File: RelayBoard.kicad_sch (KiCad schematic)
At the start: 103 parts, among them J1 CONN_03-SCREW-5MM, J11 CONN_03-SCREW-5MM, J12 CONN_03-SCREW-5MM, J13 CONN_03-SCREW-5MM, J14 CONN_03-SCREW-5MM, J15 CONN_03-SCREW-5MM, J16 CONN_03-SCREW-5MM, J17 CONN_03-SCREW-5MM, J18 CONN_03-SCREW-5MM, J2 CONN_03-SCREW-5MM, J22 Conn_01x04, J3 CONN_03-SCREW-5MM, J4 CONN_03-SCREW-5MM, J5 CONN_03-SCREW-5MM, J6 CONN_03-SCREW-5MM, J7 CONN_03-SCREW-5MM, J8 CONN_03-SCREW-5MM, J9 PJ-202A, Q1 ULN2803ADWR, Q2 ULN2803ADWR, U1 TLP148G, U11 TLP148G, U12 TLP148G, U13 TLP148G, U14 TLP148G, U15 TLP148G, U16 TLP148G, U17 TLP148G, U18 TLP148G, U2 TLP148G, U3 TLP148G, U4 TLP148G, U5 TLP148G, U6 TLP148G, U7 TLP148G, U8 TLP148G

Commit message: final touches
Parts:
- gave numbers to parts that had none: 1
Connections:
- net DC In from AC: now reaches JP1.3 (Pin_3), PS1.4 (+Vo)
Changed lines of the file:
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@@
   (junction (at 260.096 18.542) (diameter 0) (color 0 0 0 0)
   )
+  (junction (at 51.308 162.306) (diameter 0) (color 0 0 0 0)
+  )
   (junction (at 100.0115 226.06) (diameter 0) (color 0 0 0 0)
   )
@@
     (stroke (width 0) (type default) (color 0 0 0 0))
   )
+  (wire (pts (xy 51.308 165.608) (xy 51.308 162.306))
+    (stroke (width 0) (type default) (color 0 0 0 0))
+  )
   (wire (pts (xy 210.82 155.956) (xy 210.82 155.702))
     (stroke (width 0) (type default) (color 0 0 0 0))
@@
     (stroke (width 0) (type default) (color 0 0 0 0))
   )
+  (wire (pts (xy 51.308 162.306) (xy 51.562 162.306))
+    (stroke (width 0) (type default) (color 0 0 0 0))
+  )
   (polyline (pts (xy 140.97 136.906) (xy 140.97 170.561))
     (stroke (width 0.254) (type solid) (color 0 0 0 0))
@@
     (stroke (width 0) (type default) (color 0 0 0 0))
   )
-  (wire (pts (xy 49.022 162.306) (xy 51.562 162.306))
+  (wire (pts (xy 49.022 162.306) (xy 51.308 162.306))
     (stroke (width 0) (type default) (color 0 0 0 0))
   )
@@
     (stroke (width 0) (type default) (color 0 0 0 0))
   )
+  (wire (pts (xy 53.848 165.608) (xy 51.308 165.608))
+    (stroke (width 0) (type default) (color 0 0 0 0))
+  )
   (polyline (pts (xy 140.97 170.561) (xy 14.732 170.434))
     (stroke (width 0.254) (type solid) (color 0 0 0 0))
@@
     (effects (font (size 3.9878 3.9878)) (justify left bottom))
   )
+  (global_label "DC In from AC" (shape input) (at 53.848 165.608 0) (fields_autoplaced)
+    (effects (font (size 1.27 1.27)) (justify left))
+    (property "Intersheet References" "${INTERSHEET_REFS}" (id 0) (at 70.1706 165.5286 0)
+      (effects (font (size 1.27 1.27)) (justify left) hide)
+    )
+  )
   (global_label "I2C_SDA" (shape bidirectional) (at 140.716 69.85 0) (fields_autoplaced)
     (effects (font (size 1.27 1.27)) (justify left))
@@
   (symbol (lib_id "Connector:Screw_Terminal_01x02") (at 19.558 165.862 180) (unit 1)
     (in_bom yes) (on_board yes)
-    (property "Reference" "J?" (id 0) (at 19.304 158.496 0))
+    (property "Reference" "J10" (id 0) (at 19.304 158.496 0))
     (property "Value" "" (id 1) (at 19.558 160.274 0))
     (property "Footprint" "" (id 2) (at 19.558 165.862 0)
@@
       (effects (font (size 1.27 1.27)) hide)
     )
-    (property "Value" "GND" (id 1) (at 54.102 168.656 0))
+    (property "Value" "GND" (id 1) (at 52.324 169.164 0))
     (property "Footprint" "" (id 2) (at 49.022 167.386 0)
       (effects (font (size 1.27 1.27)) hide)
@@
       (reference "J9") (unit 1) (value "PJ-202A") (footprint "Connectors:POWER_JACK_PTH_LOCK")
     )
+    (path "/2c0c12a9-f7a0-4389-a8c1-bd69df364647"
+      (reference "J10") (unit 1) (value "AC In") (footprint "TerminalBlock:TerminalBlock_Altech_AK300-2_P5.00mm")
+    )
     (path "/04a15d9e-6cd5-4e20-ab11-6766c342d625"
       (reference "J11") (unit 1) (value "CONN_03-SCREW-5MM") (footprint "Connectors:SCREWTERMINAL-5MM-3")
@@
       (reference "J22") (unit 1) (value "Conn_01x04") (footprint "Connector_PinSocket_2.54mm:PinSocket_1x04_P2.54mm_Vertical")
     )
-    (path "/2c0c12a9-f7a0-4389-a8c1-bd69df364647"
-      (reference "J?") (unit 1) (value "AC In") (footprint "TerminalBlock:TerminalBlock_Altech_AK300-2_P5.00mm")
-    )
     (path "/d43d6827-1e42-4d7c-85a8-2e3c7801a7de"

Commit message: total rewrite, solid state relays & change all footprints to 0805s
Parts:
- removed J1, J11, J12, J13, J14, J15, J16, J17, J18, J2, J3, J4, J5, J6, J7, J8: CONN_03-SCREW-5MM, Connectors:SCREWTERMINAL-5MM-3, symbol SparkFun-Connectors:CONN_03-SCREW-5MM
- removed PS1: (no value), symbol Converter_ACDC:IRM-02-5
- removed Q1, Q2: ULN2803ADWR, digikey-footprints:SOIC-18_W7.5mm, symbol dk_Transistors-Bipolar-BJT-Arrays:ULN2803ADWR
- removed U1, U11, U12, U13, U14, U15, U16, U17, U18, U2, U3, U4, U5, U6, U7, U8: TLP148G, Package_SO:MFSOP6-5_4.4x3.6mm_P1.27mm, symbol Relay_SolidState:TLP148G
- removed UP1: AP1117-33, Package_TO_SOT_SMD:SOT-223-3_TabPin2, symbol Regulator_Linear:AP1117-33
- added D1, D3: D, Diode_SMD:D_0805_2012Metric, symbol Device:D
- added D11, D12, D13, D14, D15, D16, D17, D18, D2, D4, D5, D6, D7, D8: (no value), symbol Device:D
- added DR1: BAT54SLT1G, digikey-footprints:SOT-23-3, symbol dk_Diodes-Rectifiers-Arrays:BAT54SLT1G
- added J1, J11, J12, J13, J14, J15, J16, J17, J18, J2, J3, J4, J5, J6, J7, J8: OSTTC020162, digikey-footprints:Term_Block_1x2_P5mm, symbol Connector:OSTTC020162
- added J20: OSTTC020162, digikey-footprints:Term_Block_1x2_P5mm, symbol dk_Terminal-Blocks-Wire-to-Board:OSTTC020162
- added K1, K11, K12, K13, K14, K15, K16, K17, K18, K2, K3, K4, K5, K6, K7, K8: AQY212GHAX, SOP254P962X315-4N, symbol Panasonic-SSR:AQY212GHAX
- added U1: AP1117-50, Package_TO_SOT_SMD:SOT-223-3_TabPin2, symbol Regulator_Linear:AP1117-50
- D31, D32, D33, D34, D45: footprint LED_SMD:LED_0402_1005Metric -> LED_SMD:LED_0805_2012Metric
- D311: renamed from D312; footprint LED_SMD:LED_0402_1005Metric -> LED_SMD:LED_0805_2012Metric
- D312: renamed from D311; footprint LED_SMD:LED_0402_1005Metric -> LED_SMD:LED_0805_2012Metric
- D313: renamed from D314; footprint LED_SMD:LED_0402_1005Metric -> LED_SMD:LED_0805_2012Metric
- D314: renamed from D313; footprint LED_SMD:LED_0402_1005Metric -> LED_SMD:LED_0805_2012Metric
- D315: renamed from D316; footprint LED_SMD:LED_0402_1005Metric -> LED_SMD:LED_0805_2012Metric
- D316: renamed from D315; footprint LED_SMD:LED_0402_1005Metric -> LED_SMD:LED_0805_2012Metric
- D317: renamed from D318; footprint LED_SMD:LED_0402_1005Metric -> LED_SMD:LED_0805_2012Metric
- D318: renamed from D317; footprint LED_SMD:LED_0402_1005Metric -> LED_SMD:LED_0805_2012Metric
- D35: renamed from D36; footprint LED_SMD:LED_0402_1005Metric -> LED_SMD:LED_0805_2012Metric
- D36: renamed from D35; footprint LED_SMD:LED_0402_1005Metric -> LED_SMD:LED_0805_2012Metric
- D37: renamed from D38; footprint LED_SMD:LED_0402_1005Metric -> LED_SMD:LED_0805_2012Metric
- D38: renamed from D37; footprint LED_SMD:LED_0402_1005Metric -> LED_SMD:LED_0805_2012Metric
- J10: value (none) -> 24VAC In; footprint (none) -> digikey-footprints:Term_Block_1x2_P5mm; symbol Connector:Screw_Terminal_01x02 -> Connector:OSTTC020162
- J19: value (none) -> Raspberry_Pi_2_3; footprint (none) -> Connector_PinHeader_2.54mm:PinHeader_2x20_P2.54mm_Vertical
- J9: footprint Connectors:POWER_JACK_PTH_LOCK -> digikey-footprints:Barrel_Jack_5.5mmODx2.1mmID_PJ-202A
- JP1: value (none) -> VBUS Select; footprint (none) -> Connector_PinHeader_2.54mm:PinHeader_2x02_P2.54mm_Vertical
- R101, R102, R103, R104, R11, R201, R202, R203, R204, R4, R5: footprint Resistor_SMD:R_0402_1005Metric -> Resistor_SMD:R_0805_2012Metric
- R105: renamed from R106; footprint Resistor_SMD:R_0402_1005Metric -> Resistor_SMD:R_0805_2012Metric
- R106: renamed from R105; footprint Resistor_SMD:R_0402_1005Metric -> Resistor_SMD:R_0805_2012Metric
- R107: renamed from R108; footprint Resistor_SMD:R_0402_1005Metric -> Resistor_SMD:R_0805_2012Metric
- R108: renamed from R107; footprint Resistor_SMD:R_0402_1005Metric -> Resistor_SMD:R_0805_2012Metric
- R111: renamed from R112; footprint Resistor_SMD:R_0402_1005Metric -> Resistor_SMD:R_0805_2012Metric
- R112: renamed from R111; footprint Resistor_SMD:R_0402_1005Metric -> Resistor_SMD:R_0805_2012Metric
- R113: renamed from R114; footprint Resistor_SMD:R_0402_1005Metric -> Resistor_SMD:R_0805_2012Metric
- R114: renamed from R113; footprint Resistor_SMD:R_0402_1005Metric -> Resistor_SMD:R_0805_2012Metric
- R115: renamed from R116; footprint Resistor_SMD:R_0402_1005Metric -> Resistor_SMD:R_0805_2012Metric
- R116: renamed from R115; footprint Resistor_SMD:R_0402_1005Metric -> Resistor_SMD:R_0805_2012Metric
- R117: renamed from R118; footprint Resistor_SMD:R_0402_1005Metric -> Resistor_SMD:R_0805_2012Metric
- R118: renamed from R117; footprint Resistor_SMD:R_0402_1005Metric -> Resistor_SMD:R_0805_2012Metric
- R205: renamed from R206; footprint Resistor_SMD:R_0402_1005Metric -> Resistor_SMD:R_0805_2012Metric
- R206: renamed from R205; footprint Resistor_SMD:R_0402_1005Metric -> Resistor_SMD:R_0805_2012Metric
- R207: renamed from R208; footprint Resistor_SMD:R_0402_1005Metric -> Resistor_SMD:R_0805_2012Metric
- R208: renamed from R207; footprint Resistor_SMD:R_0402_1005Metric -> Resistor_SMD:R_0805_2012Metric
- R211: renamed from R212; footprint Resistor_SMD:R_0402_1005Metric -> Resistor_SMD:R_0805_2012Metric
- R212: renamed from R211; footprint Resistor_SMD:R_0402_1005Metric -> Resistor_SMD:R_0805_2012Metric
- R213: renamed from R214; footprint Resistor_SMD:R_0402_1005Metric -> Resistor_SMD:R_0805_2012Metric
- R214: renamed from R213; footprint Resistor_SMD:R_0402_1005Metric -> Resistor_SMD:R_0805_2012Metric
- R215: renamed from R216; footprint Resistor_SMD:R_0402_1005Metric -> Resistor_SMD:R_0805_2012Metric
- R216: renamed from R215; footprint Resistor_SMD:R_0402_1005Metric -> Resistor_SMD:R_0805_2012Metric
- R217: renamed from R218; footprint Resistor_SMD:R_0402_1005Metric -> Resistor_SMD:R_0805_2012Metric
- R218: renamed from R217; footprint Resistor_SMD:R_0402_1005Metric -> Resistor_SMD:R_0805_2012Metric
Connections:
- net +3V3: now also J19.1 (3V3), J19.17 (3V3); no longer C5.1, C6.1, C7.1, C8.1, L2.2
- net AC_L_In: now also DR1.1, J20.2
- net AC_N_In: now also DR1.2, J20.1
- net GND: now also U1.1 (GND)
- net VBUS: no longer J19.2 (5V), J19.4 (5V)
- net at D34.2 (A): now also K4.2 (K)
- net at R113.1: now also J19.21 (MISO0/GPIO9), K13.1 (A)
- net at R103.1: now also J19.12 (GPIO18/PWM0), K3.1 (A)
- net at D33.2 (A): now also K3.2 (K)
- net at D38.2 (A): now also K8.2 (K)
- net at R107.1: now also J19.8 (GPIO14/TXD), K7.1 (A)
- net at D37.2 (A): now also K7.2 (K)
- net 5V: now reaches C4.1, L2.1
- net 5V: now also J19.2 (5V), J19.4 (5V), U1.2 (VO)
- net at C2.1, C3.1, L1.2: now also U1.3 (VI)
- net at D32.2 (A): now also K2.2 (K)
- net at D316.2 (A): now also K16.2 (K)
- net at R118.1: now also J19.32 (PWM0/GPIO12), K18.1 (A)
- net at R104.1: now also J19.35 (GPIO19/MISO1), K4.1 (A)
- net at R111.1: now also J19.31 (GCLK2/GPIO6), K11.1 (A)
- net at J19.29 (GCLK1/GPIO5): now also R112.1, K12.1 (A)
- net at R117.1: now also J19.33 (PWM1/GPIO13), K17.1 (A)
- net at R115.1: now also J19.23 (SCLK0/GPIO11), K15.1 (A)
- net at R116.1: now also J19.19 (MOSI0/GPIO10), K16.1 (A)
- net at R114.1: now also J19.26 (~{CE1}/GPIO7), K14.1 (A)
- net at D36.2 (A): now also K6.2 (K)
- net at D35.2 (A): now also K5.2 (K)
- net at R101.1: now also J19.40 (GPIO21/SCLK1), K1.1 (A)
- net at R102.1: now also J19.38 (GPIO20/MOSI1), K2.1 (A)
- net at D318.2 (A): now also K18.2 (K)
- net at J19.10 (GPIO15/RXD): now also R108.1, K8.1 (A)
- net at J19.11 (GPIO17): now also R106.1, K6.1 (A)
- net at J19.36 (GPIO16): now also R105.1, K5.1 (A)
- net at D317.2 (A): now also K17.2 (K)
- net at D315.2 (A): now also K15.2 (K)
- net at D313.2 (A): now also K13.2 (K)
- net at D311.2 (A): now also K11.2 (K)
- net at D312.2 (A): now also K12.2 (K)
- net at D314.2 (A): now also K14.2 (K)
- net at D31.2 (A): now also K1.2 (K)
- net DC In from AC renamed 16VDC Unregulated In from AC
- net 16VDC Unregulated In from AC: now also DR1.3
- new net: D5.2 (A), J5.1 (Pin_1), K5.4 (D2)
- new net: D5.1 (K), J5.2 (Pin_2), K5.3 (D1)
- new net: D15.1 (K), J15.2 (Pin_2), K15.3 (D1)
- new net: D15.2 (A), J15.1 (Pin_1), K15.4 (D2)
- new net: D11.1 (K), J11.2 (Pin_2), K11.3 (D1)
- new net: D11.2 (A), J11.1 (Pin_1), K11.4 (D2)
- new net: D13.1 (K), J13.2 (Pin_2), K13.3 (D1)
- new net: D13.2 (A), J13.1 (Pin_1), K13.4 (D2)
- new net: D18.2 (A), J18.1 (Pin_1), K18.4 (D2)
- new net: D18.1 (K), J18.2 (Pin_2), K18.3 (D1)
- new net: D3.1 (K), J3.2 (Pin_2), K3.3 (D1)
- new net: D3.2 (A), J3.1 (Pin_1), K3.4 (D2)
- new net: C5.1, C6.1, C7.1, C8.1, L2.2
- new net: D6.1 (K), J6.2 (Pin_2), K6.3 (D1)
- new net: D6.2 (A), J6.1 (Pin_1), K6.4 (D2)
- new net: D4.1 (K), J4.2 (Pin_2), K4.3 (D1)
- new net: D4.2 (A), J4.1 (Pin_1), K4.4 (D2)
- new net: D2.2 (A), J2.1 (Pin_1), K2.4 (D2)
- new net: D2.1 (K), J2.2 (Pin_2), K2.3 (D1)
- new net: D7.1 (K), J7.2 (Pin_2), K7.3 (D1)
- new net: D7.2 (A), J7.1 (Pin_1), K7.4 (D2)
- new net: D8.1 (K), J8.2 (Pin_2), K8.3 (D1)
- new net: D8.2 (A), J8.1 (Pin_1), K8.4 (D2)
- new net: D1.1 (K), J1.2 (Pin_2), K1.3 (D1)
- new net: D1.2 (A), J1.1 (Pin_1), K1.4 (D2)
- new net: D17.1 (K), J17.2 (Pin_2), K17.3 (D1)
- new net: D17.2 (A), J17.1 (Pin_1), K17.4 (D2)
- new net: D12.1 (K), J12.2 (Pin_2), K12.3 (D1)
- new net: D12.2 (A), J12.1 (Pin_1), K12.4 (D2)
- new net: D16.2 (A), J16.1 (Pin_1), K16.4 (D2)
- new net: D16.1 (K), J16.2 (Pin_2), K16.3 (D1)
- new net: D14.1 (K), J14.2 (Pin_2), K14.3 (D1)
- new net: D14.2 (A), J14.1 (Pin_1), K14.4 (D2)
- no-connect marks 3 -> 1
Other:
- moved on the sheet: D312, D313, D314, D315, D316, D317, D318, D32, D33, D34, D35, D36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

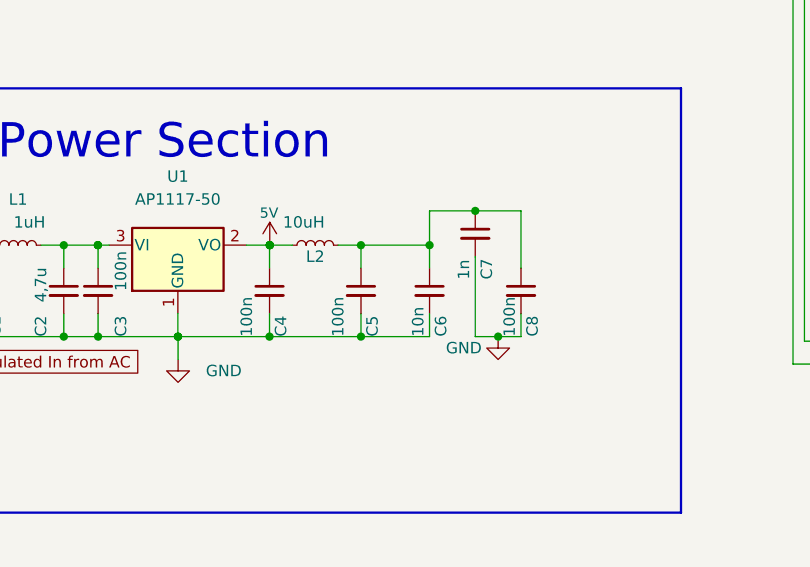
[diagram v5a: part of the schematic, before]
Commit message: fix drc errors, change bottom zone to GND
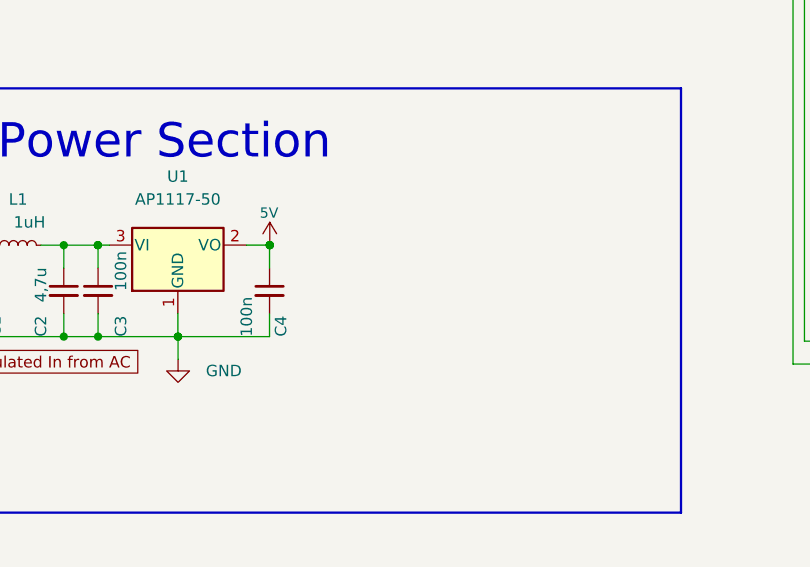
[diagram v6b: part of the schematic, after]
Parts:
- removed C5: 100n, Capacitor_SMD:C_0805_2012Metric, symbol Device:C_Small
- removed C6: 10n, Capacitor_SMD:C_0805_2012Metric, symbol Device:C_Small
- removed C7: 1n, Capacitor_SMD:C_0603_1608Metric, symbol Device:C_Small
- removed C8: 100n, Capacitor_SMD:C_0603_1608Metric, symbol Device:C_Small
- removed L2: 10uH, Inductor_SMD:L_0805_2012Metric, symbol Device:L_Small

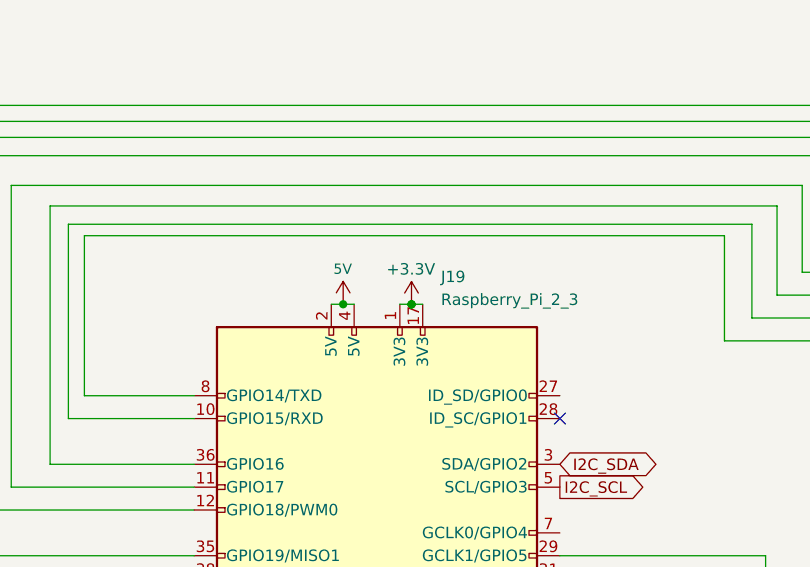
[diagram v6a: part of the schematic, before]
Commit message: resize board
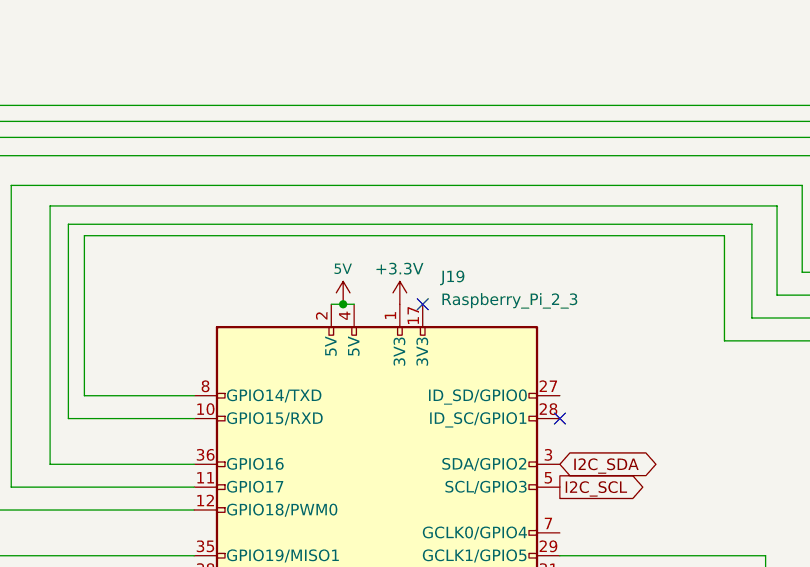
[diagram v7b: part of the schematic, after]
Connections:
- net +3V3: no longer J19.17 (3V3)
- no-connect marks 1 -> 2
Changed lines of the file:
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@@
   (junction (at 306.1462 79.2226) (diameter 0) (color 0 0 0 0)
   )
-  (junction (at 124.2314 52.0954) (diameter 0) (color 0 0 0 0)
-  )
   (junction (at 306.1462 52.1716) (diameter 0) (color 0 0 0 0)
   )
@@
   (junction (at 382.8034 79.3242) (diameter 0) (color 0 0 0 0)
   )
-  (junction (at 124.2314 52.07) (diameter 0) (color 0 0 0 0)
-  )
   (junction (at 306.07 219.4814) (diameter 0) (color 0 0 0 0)
   )
@@
   (junction (at 51.308 163.0426) (diameter 0) (color 0 0 0 0)
   )
+  (no_connect (at 125.476 52.07))
   (no_connect (at 140.716 64.77))
   (wire (pts (xy 243.332 175.26) (xy 243.332 205.486))
@@
     (stroke (width 0) (type default) (color 0 0 0 0))
   )
-  (wire (pts (xy 124.2314 52.07) (xy 124.2314 52.0954))
-    (stroke (width 0) (type default) (color 0 0 0 0))
-  )
   (wire (pts (xy 159.004 44.45) (xy 87.884 44.45))
     (stroke (width 0) (type default) (color 0 0 0 0))
@@
     (stroke (width 0) (type default) (color 0 0 0 0))
   )
-  (wire (pts (xy 122.936 52.07) (xy 124.2314 52.07))
-    (stroke (width 0) (type default) (color 0 0 0 0))
-  )
   (wire (pts (xy 356.4663 216.6366) (xy 356.4663 210.82))
     (stroke (width 0) (type default) (color 0 0 0 0))
@@
     (stroke (width 0) (type default) (color 0 0 0 0))
   )
-  (wire (pts (xy 124.2314 52.07) (xy 125.476 52.07))
-    (stroke (width 0) (type default) (color 0 0 0 0))
-  )
   (wire (pts (xy 246.634 134.62) (xy 246.634 123.19))
     (stroke (width 0) (type default) (color 0 0 0 0))
@@
     (pin "2")
   )
-  (symbol (lib_id "power:+3.3V") (at 124.2314 52.0954 0) (unit 1)
+  (symbol (lib_id "power:+3.3V") (at 122.936 52.07 0) (unit 1)
     (in_bom yes) (on_board yes)
-    (property "Reference" "#PWR0104" (id 0) (at 124.2314 55.9054 0)
+    (property "Reference" "#PWR0104" (id 0) (at 122.936 55.88 0)
       (effects (font (size 1.27 1.27)) hide)
     )
-    (property "Value" "+3.3V" (id 1) (at 124.1552 48.1838 0))
-    (property "Footprint" "" (id 2) (at 124.2314 52.0954 0)
+    (property "Value" "+3.3V" (id 1) (at 122.8598 48.1584 0))
+    (property "Footprint" "" (id 2) (at 122.936 52.07 0)
       (effects (font (size 1.27 1.27)) hide)
     )
-    (property "Datasheet" "" (id 3) (at 124.2314 52.0954 0)
+    (property "Datasheet" "" (id 3) (at 122.936 52.07 0)
       (effects (font (size 1.27 1.27)) hide)
     )
